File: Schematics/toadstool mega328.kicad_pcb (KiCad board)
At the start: 2 copper layers, 49.5 x 81.2 mm, 25 parts, among them CON1 BARREL_JACK, IC1 ATMEGA328P-P, K1 SHIELD, K2 V-SELECT, K4 ICSP, K5 PIN 2-8, K6 PIN 21-28, K7 XTAL, K8 PIN 15-19, K9 PIN 11-14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

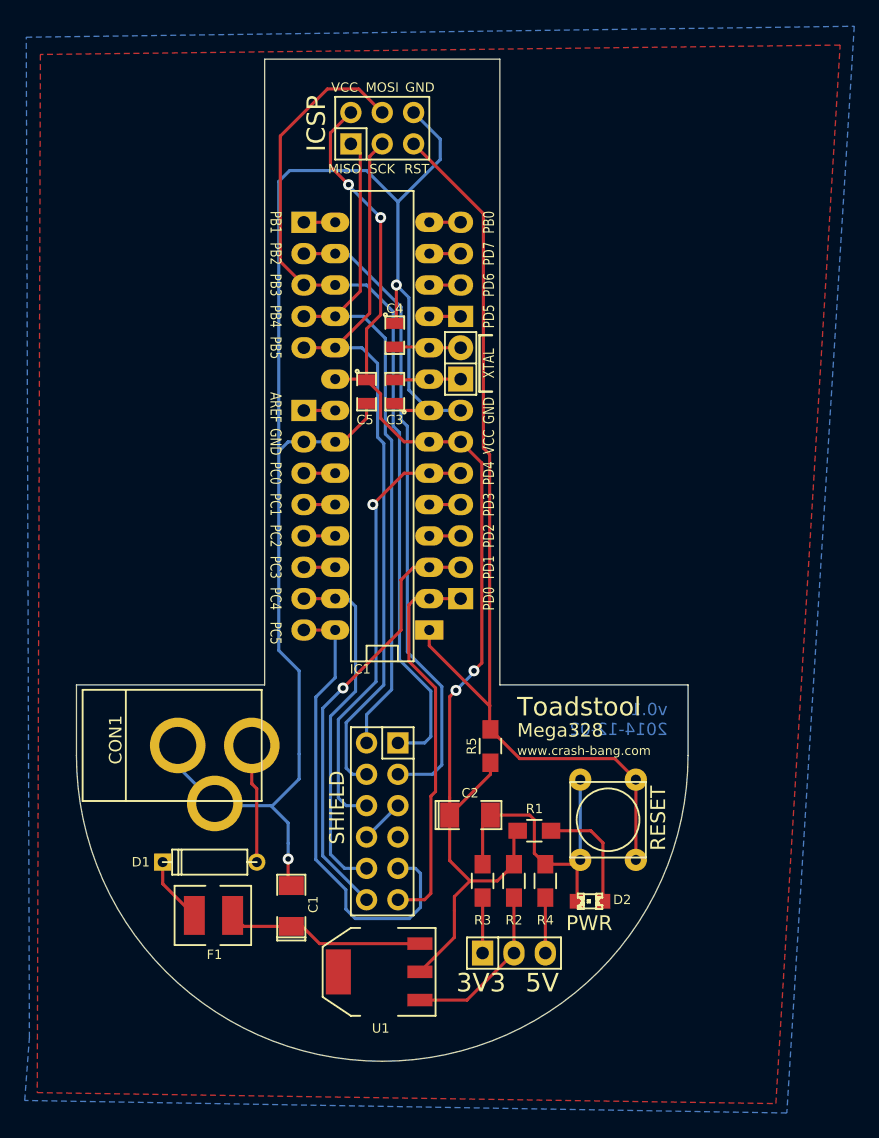
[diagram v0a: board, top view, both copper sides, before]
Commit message: Cosmetic
Rounding of board corners
Change logo
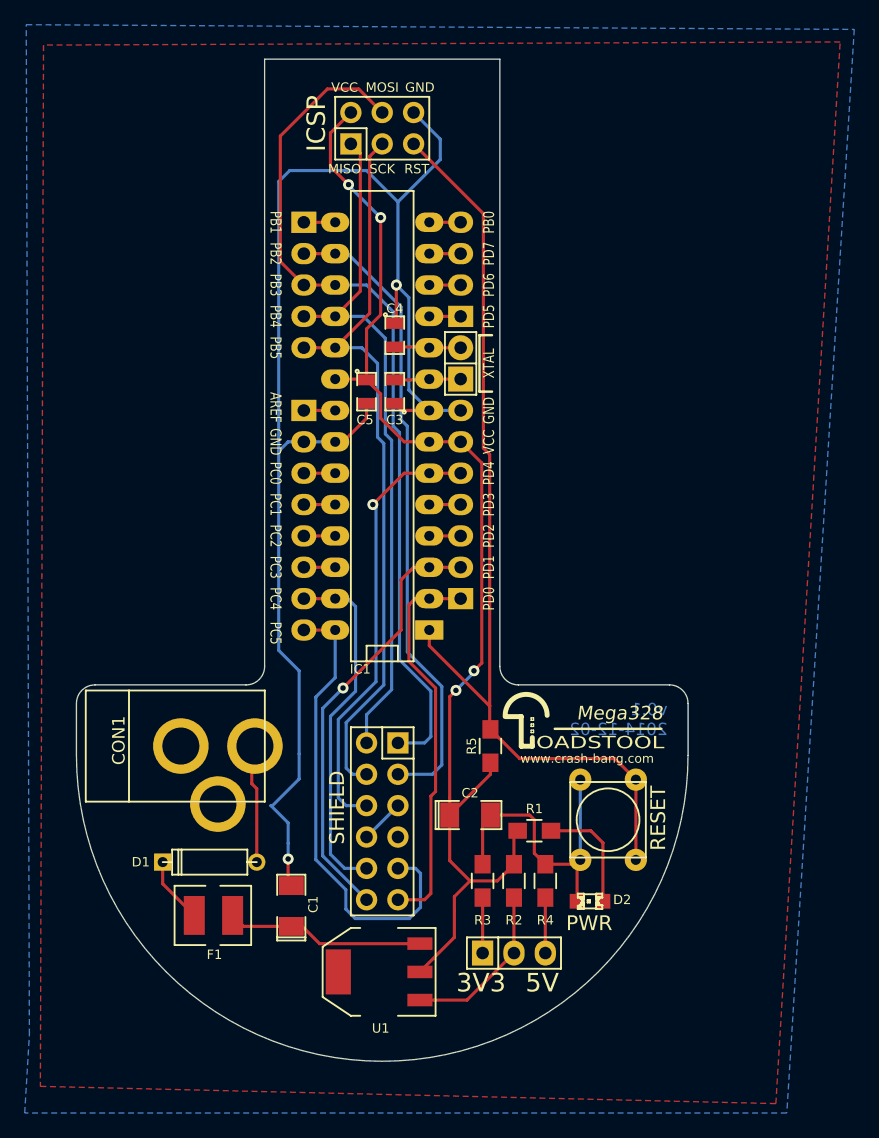
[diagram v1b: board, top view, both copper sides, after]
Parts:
- added Toadstool_Logo: LOGO**, Toadstool:Toadstool_Logo, F.Cu at (224.5, 101.1)
- moved CON1 0.26 mm to (191.8, 103.4)
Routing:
- net GND: track 157.1 -> 144.7 mm
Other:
- outline, holes or cut-outs redrawn
- board text removed: "Toadstool"

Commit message: Components Changed
Updated Power Jack and Reset button with 3D models.
Minor changes to silkscreen
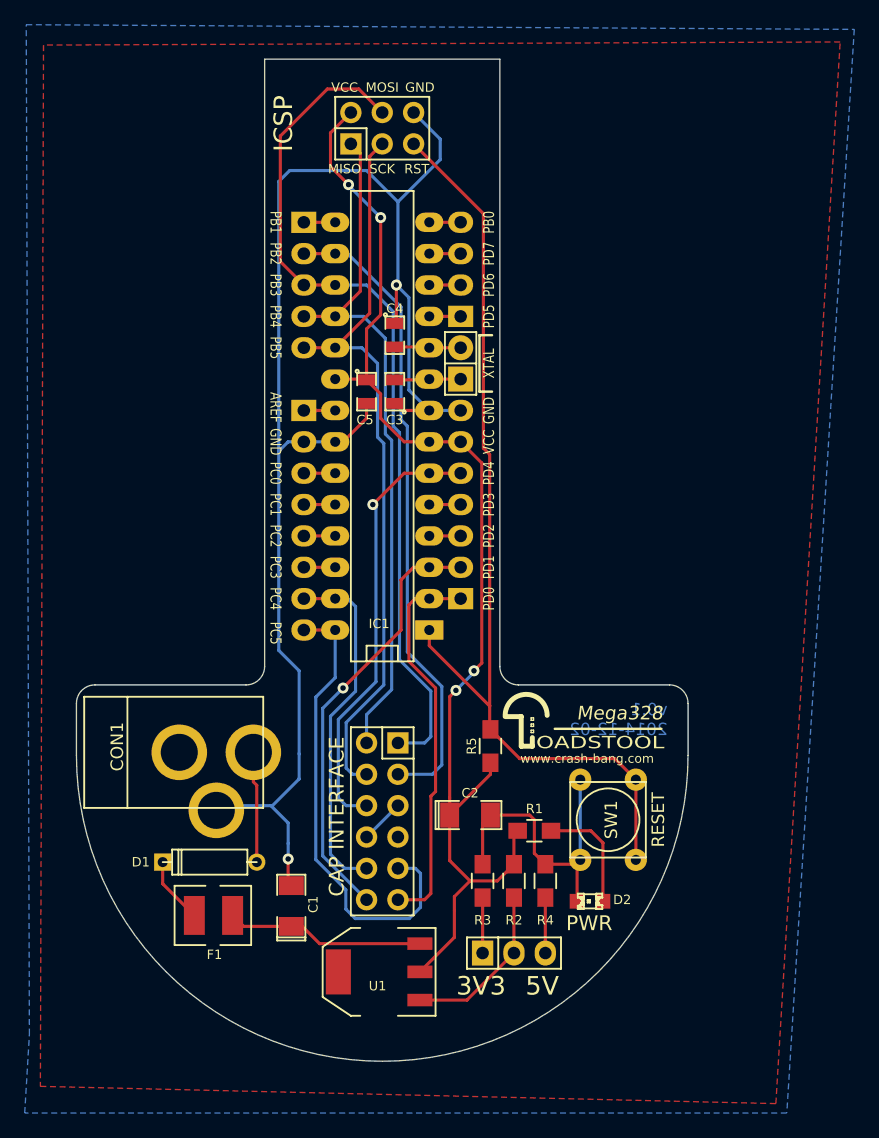
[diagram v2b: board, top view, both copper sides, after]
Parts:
- K1: value SHIELD -> CAP INTERFACE
- U1: footprint SMD_Packages:SOT-223 -> SOT-223
- moved CON1 0.52 mm to (191.6, 103.9)
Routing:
- net GND: track 144.7 -> 149.3 mm
